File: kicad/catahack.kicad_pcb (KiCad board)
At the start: 4 copper layers, 100 x 100 mm, 175 parts, among them J1 XCVR power choice, J10 PC_AUDIO_EXTRA, J11 Jack header, J12 Jack header, J13 L/R channel choice, J14 Jack header, J15 CITA/OMTP choice, J16 TRRS/TRS+TS choice, J18 Xcvr grounding jumpers, J19 XCVR_Audio, J2 USB_B, J3 FTDI header, J4 PTT choice, J5 XCVR_CAT_TTL, J6 XCVR_PTT, J7 XCVR_CAT_RS232, J8 PC_AUDIO_IO, J9 PC_AUDIO_OUT, T1 T6003NL, T2 T6003NL, U1 PQS075-S5-S5-S, U2 L78M05CDT-TR, U3 SN65220, U4 Si8663AB-B-IS1, U5 FT232RL, U6 SN74HCT32D, U7 VOR1121B6T, U8 MAX3387ECUG+

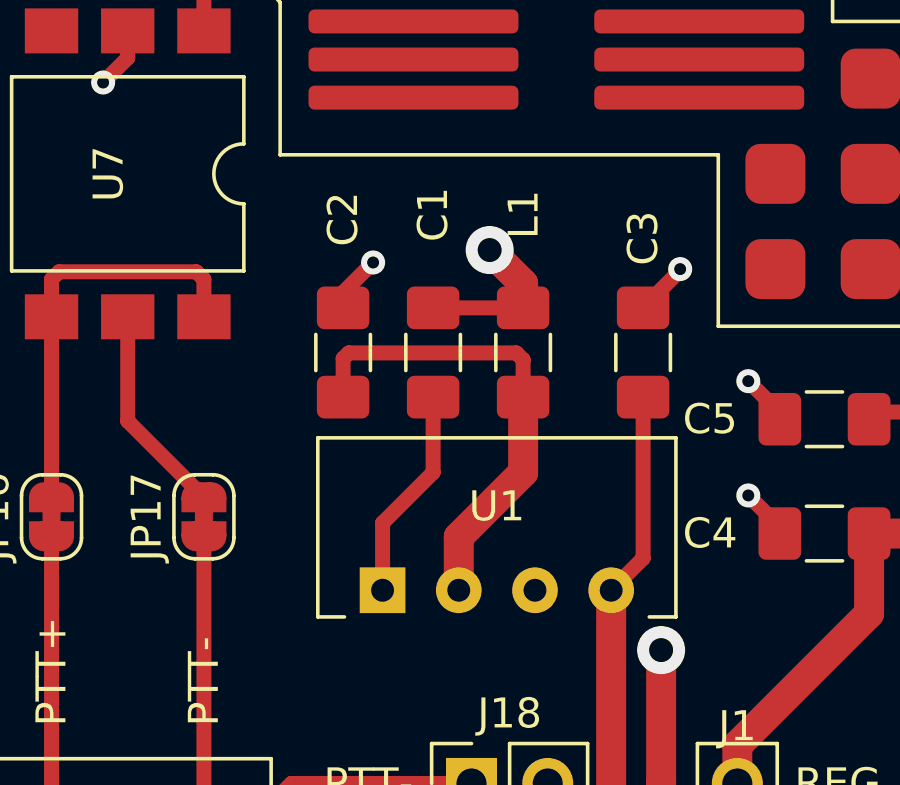
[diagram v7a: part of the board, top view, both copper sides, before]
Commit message: Changed L1 to 0805 due to stock issues
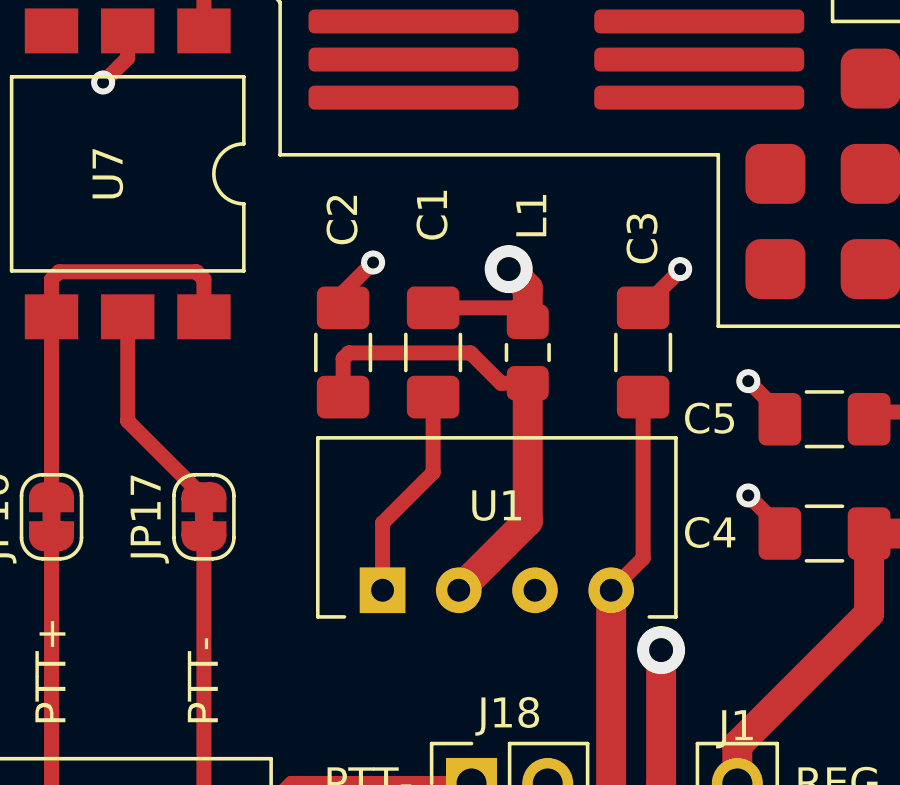
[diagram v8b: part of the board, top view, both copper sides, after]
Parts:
- L1: footprint Inductor_SMD:L_1206_3216Metric_Pad1.42x1.75mm_HandSolder -> Inductor_SMD:L_0805_2012Metric_Pad1.15x1.40mm_HandSolder
- moved L1 0.16 mm to (97.2, 112.0)
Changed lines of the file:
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@@
   )
   (setup
-    (last_trace_width 0.3)
+    (last_trace_width 0.5)
     (user_trace_width 0.261)
     (user_trace_width 0.3)
@@
     (add_net XCVR_TXD_DRV)
   )
+  (module Inductor_SMD:L_0805_2012Metric_Pad1.15x1.40mm_HandSolder (layer F.Cu)
+    (at 97.155 112 90)
+    (descr "Capacitor SMD 0805 (2012 Metric), square (rectangular) end terminal, IPC_7351 nominal with elongated pad for handsoldering. (Body size source: https://docs.google.com/spreadsheets/d/1BsfQQcO9C6DZCsRaXUlFlo91Tg2WpOkGARC1WS5S8t0/edit?usp=sharing), generated with kicad-footprint-generator")
+    (tags "inductor handsolder")
+    (attr smd)
+    (fp_text reference L1 (at 4.558 0.155 90) (layer F.SilkS)
+      (effects (font (size 1 1) (thickness 0.15)))
+    )
+    (fp_text value 6.8u (at 0 1.65 90) (layer F.Fab)
+      (effects (font (size 1 1) (thickness 0.15)))
+    )
+    (fp_text user %R (at 0 0 90) (layer F.Fab)
+      (effects (font (size 0.5 0.5) (thickness 0.08)))
+    )
+    (fp_line (start 1.85 0.95) (end -1.85 0.95) (layer F.CrtYd) (width 0.05))
+    (fp_line (start 1.85 -0.95) (end 1.85 0.95) (layer F.CrtYd) (width 0.05))
+    (fp_line (start -1.85 -0.95) (end 1.85 -0.95) (layer F.CrtYd) (width 0.05))
+    (fp_line (start -1.85 0.95) (end -1.85 -0.95) (layer F.CrtYd) (width 0.05))
+    (fp_line (start -0.261252 0.71) (end 0.261252 0.71) (layer F.SilkS) (width 0.12))
+    (fp_line (start -0.261252 -0.71) (end 0.261252 -0.71) (layer F.SilkS) (width 0.12))
+    (fp_line (start 1 0.6) (end -1 0.6) (layer F.Fab) (width 0.1))
+    (fp_line (start 1 -0.6) (end 1 0.6) (layer F.Fab) (width 0.1))
+    (fp_line (start -1 -0.6) (end 1 -0.6) (layer F.Fab) (width 0.1))
+    (fp_line (start -1 0.6) (end -1 -0.6) (layer F.Fab) (width 0.1))
+    (pad 2 smd roundrect (at 1.025 0 90) (size 1.15 1.4) (layers F.Cu F.Paste F.Mask) (roundrect_rratio 0.217391)
+      (net 1 VCC))
+    (pad 1 smd roundrect (at -1.025 0 90) (size 1.15 1.4) (layers F.Cu F.Paste F.Mask) (roundrect_rratio 0.217391)
+      (net 3 "Net-(C2-Pad2)"))
+    (model ${KISYS3DMOD}/Inductor_SMD.3dshapes/L_0805_2012Metric.wrl
+      (at (xyz 0 0 0))
+      (scale (xyz 1 1 1))
+      (rotate (xyz 0 0 0))
+    )
+  )
   (module Resistor_SMD:R_1206_3216Metric_Pad1.42x1.75mm_HandSolder (layer F.Cu)
     (at 112.395 54.61)
@@
     )
   )
-  (module Inductor_SMD:L_1206_3216Metric_Pad1.42x1.75mm_HandSolder (layer F.Cu)
-    (at 97 112 90)
-    (descr "Capacitor SMD 1206 (3216 Metric), square (rectangular) end terminal, IPC_7351 nominal with elongated pad for handsoldering. (Body size source: http://www.tortai-tech.com/upload/download/2011102023233369053.pdf), generated with kicad-footprint-generator")
-    (tags "inductor handsolder")
-    (attr smd)
-    (fp_text reference L1 (at 4.6 0.02 90) (layer F.SilkS)
-      (effects (font (size 1 1) (thickness 0.15)))
-    )
-    (fp_text value 6.8u (at 0 1.82 90) (layer F.Fab)
-      (effects (font (size 1 1) (thickness 0.15)))
-    )
-    (fp_text user %R (at 0 0 90) (layer F.Fab)
-      (effects (font (size 0.8 0.8) (thickness 0.12)))
-    )
-    (fp_line (start 2.45 1.12) (end -2.45 1.12) (layer F.CrtYd) (width 0.05))
-    (fp_line (start 2.45 -1.12) (end 2.45 1.12) (layer F.CrtYd) (width 0.05))
-    (fp_line (start -2.45 -1.12) (end 2.45 -1.12) (layer F.CrtYd) (width 0.05))
-    (fp_line (start -2.45 1.12) (end -2.45 -1.12) (layer F.CrtYd) (width 0.05))
-    (fp_line (start -0.602064 0.91) (end 0.602064 0.91) (layer F.SilkS) (width 0.12))
-    (fp_line (start -0.602064 -0.91) (end 0.602064 -0.91) (layer F.SilkS) (width 0.12))
-    (fp_line (start 1.6 0.8) (end -1.6 0.8) (layer F.Fab) (width 0.1))
-    (fp_line (start 1.6 -0.8) (end 1.6 0.8) (layer F.Fab) (width 0.1))
-    (fp_line (start -1.6 -0.8) (end 1.6 -0.8) (layer F.Fab) (width 0.1))
-    (fp_line (start -1.6 0.8) (end -1.6 -0.8) (layer F.Fab) (width 0.1))
-    (pad 2 smd roundrect (at 1.4875 0 90) (size 1.425 1.75) (layers F.Cu F.Paste F.Mask) (roundrect_rratio 0.175439)
-      (net 1 VCC))
-    (pad 1 smd roundrect (at -1.4875 0 90) (size 1.425 1.75) (layers F.Cu F.Paste F.Mask) (roundrect_rratio 0.175439)
-      (net 3 "Net-(C2-Pad2)"))
-    (model ${KISYS3DMOD}/Inductor_SMD.3dshapes/L_1206_3216Metric.wrl
-      (at (xyz 0 0 0))
-      (scale (xyz 1 1 1))
-      (rotate (xyz 0 0 0))
-    )
-  )
   (module Package_TO_SOT_SMD:SOT-23-6_Handsoldering (layer F.Cu)
     (at 32.7025 67.2465)
@@
   (via (at 52.07 43.18) (size 0.8) (drill 0.4) (layers F.Cu B.Cu) (net 1))
   (segment (start 52.07 41.4925) (end 52.07 43.18) (width 0.5) (layer F.Cu) (net 1))
-  (segment (start 97 110.5125) (end 94 110.5125) (width 0.5) (layer F.Cu) (net 1))
-  (via (at 95.885 108.585) (size 1.6) (drill 0.8) (layers F.Cu B.Cu) (net 1))
-  (segment (start 97 110.5125) (end 97 109.7) (width 1) (layer F.Cu) (net 1))
-  (segment (start 97 109.7) (end 95.885 108.585) (width 1) (layer F.Cu) (net 1))
   (segment (start 64.135 39.37) (end 64.135 40.64) (width 0.5) (layer B.Cu) (net 1))
   (via (at 63.5 41.275) (size 0.8) (drill 0.4) (layers F.Cu B.Cu) (net 1))
@@
   (segment (start 36.703 72.517) (end 37.719999 71.500001) (width 0.3) (layer F.Cu) (net 1))
   (via (at 36.703 72.517) (size 0.8) (drill 0.4) (layers F.Cu B.Cu) (net 1))
+  (via (at 96.52 109.22) (size 1.6) (drill 0.8) (layers F.Cu B.Cu) (net 1))
+  (segment (start 97.155 110.975) (end 97.155 109.855) (width 1) (layer F.Cu) (net 1))
+  (segment (start 97.155 109.855) (end 96.52 109.22) (width 1) (layer F.Cu) (net 1))
+  (segment (start 96.6925 110.5125) (end 97.155 110.975) (width 0.5) (layer F.Cu) (net 1))
+  (segment (start 94 110.5125) (end 96.6925 110.5125) (width 0.5) (layer F.Cu) (net 1))
   (via (at 29.972 73.533) (size 0.8) (drill 0.4) (layers F.Cu B.Cu) (net 2))
   (segment (start 31.6595 73.533) (end 29.972 73.533) (width 0.5) (layer F.Cu) (net 2))
@@
   (segment (start 38.945 68.845) (end 40.27 68.845) (width 0.3) (layer F.Cu) (net 2))
   (segment (start 40.27 68.845) (end 40.64 69.215) (width 0.3) (layer F.Cu) (net 2))
-  (segment (start 97 113.4875) (end 97 116) (width 1) (layer F.Cu) (net 3))
-  (segment (start 94.855 118.145) (end 94.855 119.925) (width 1) (layer F.Cu) (net 3))
-  (segment (start 97 116) (end 94.855 118.145) (width 1) (layer F.Cu) (net 3))
-  (segment (start 91.186 112.014) (end 96.774 112.014) (width 0.5) (layer F.Cu) (net 3))
-  (segment (start 97 112.24) (end 97 113.4875) (width 0.5) (layer F.Cu) (net 3))
-  (segment (start 96.774 112.014) (end 97 112.24) (width 0.5) (layer F.Cu) (net 3))
-  (segment (start 91 113.4875) (end 91 112.2) (width 0.5) (layer F.Cu) (net 3))
-  (segment (start 91 112.2) (end 91.186 112.014) (width 0.5) (layer F.Cu) (net 3))
+  (segment (start 97.155 117.625) (end 97.155 113.025) (width 1) (layer F.Cu) (net 3))
+  (segment (start 94.855 119.925) (end 97.155 117.625) (width 1) (layer F.Cu) (net 3))
+  (segment (start 91.186 112.014) (end 91 112.2) (width 0.5) (layer F.Cu) (net 3))
+  (segment (start 95.25 112.014) (end 91.186 112.014) (width 0.5) (layer F.Cu) (net 3))
+  (segment (start 91 112.2) (end 91 113.4875) (width 0.5) (layer F.Cu) (net 3))
+  (segment (start 97.155 113.025) (end 96.261 113.025) (width 0.5) (layer F.Cu) (net 3))
+  (segment (start 96.261 113.025) (end 95.25 112.014) (width 0.5) (layer F.Cu) (net 3))
   (via (at 107.95 97.155) (size 0.8) (drill 0.4) (layers F.Cu B.Cu) (net 4))
   (segment (start 109.6375 97.155) (end 107.95 97.155) (width 0.5) (layer F.Cu) (net 4))
